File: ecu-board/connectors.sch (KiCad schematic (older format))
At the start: 19 parts, among them J10 Injector connector, J11 MAP connector, J13 Chrankshaft Hall connector, J14 Camshaft Hall connector, J15 EGO connector, J2 Battery power conenctor, J3 Button input connector, J4 Motor conenctor, J5 Serial DB9 connector, J6 Ignition 1 connector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

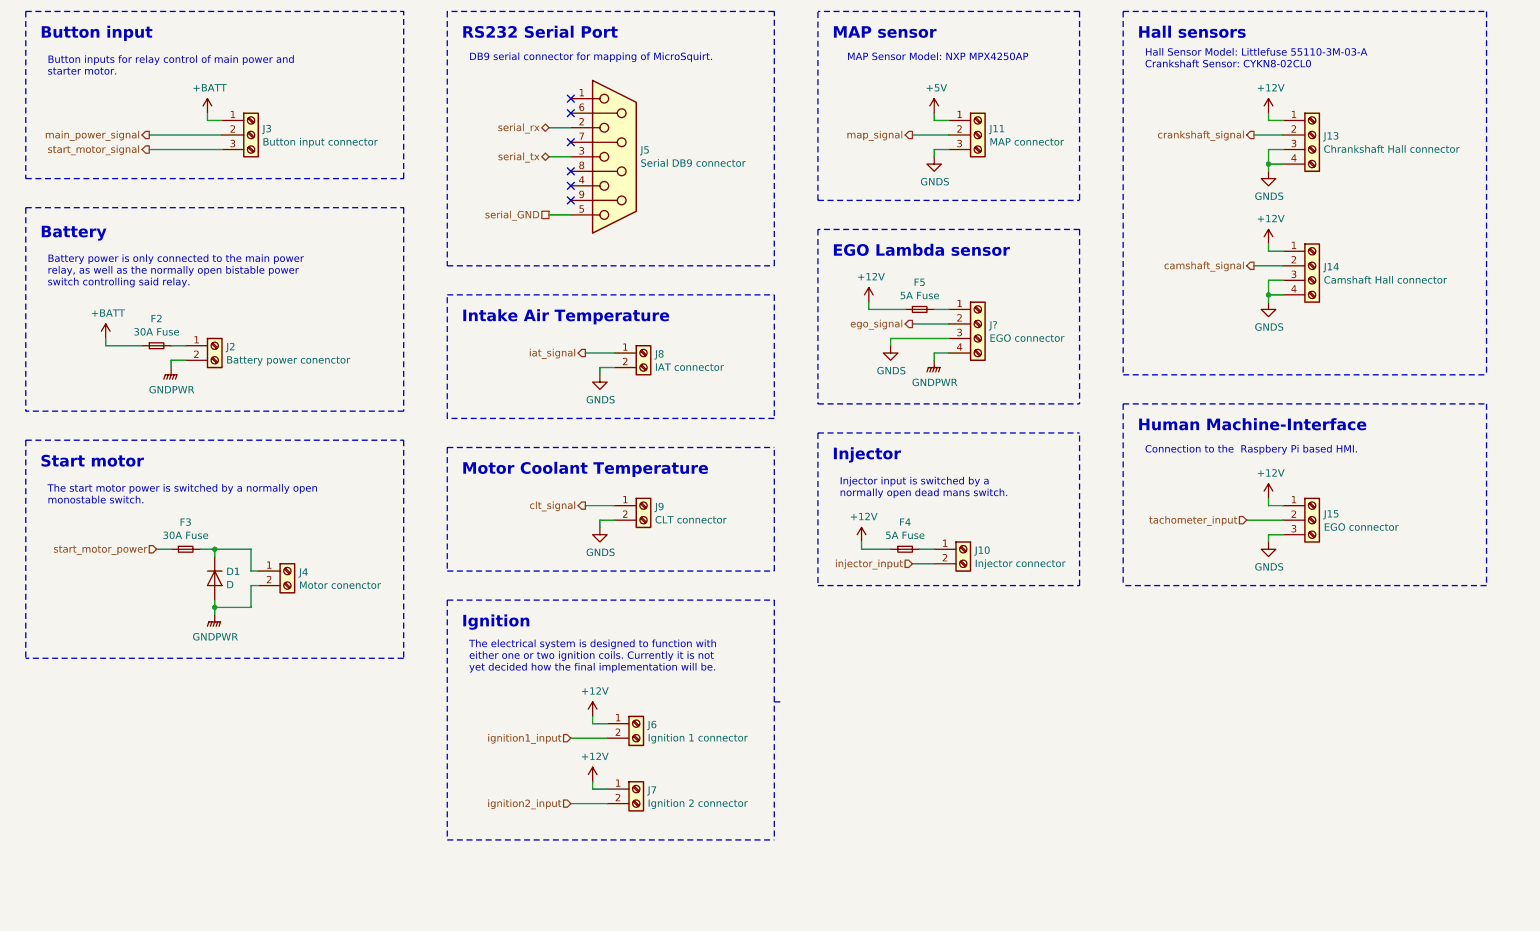
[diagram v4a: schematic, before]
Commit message: Mount MAP sensor to PCB. Reverse injector input.
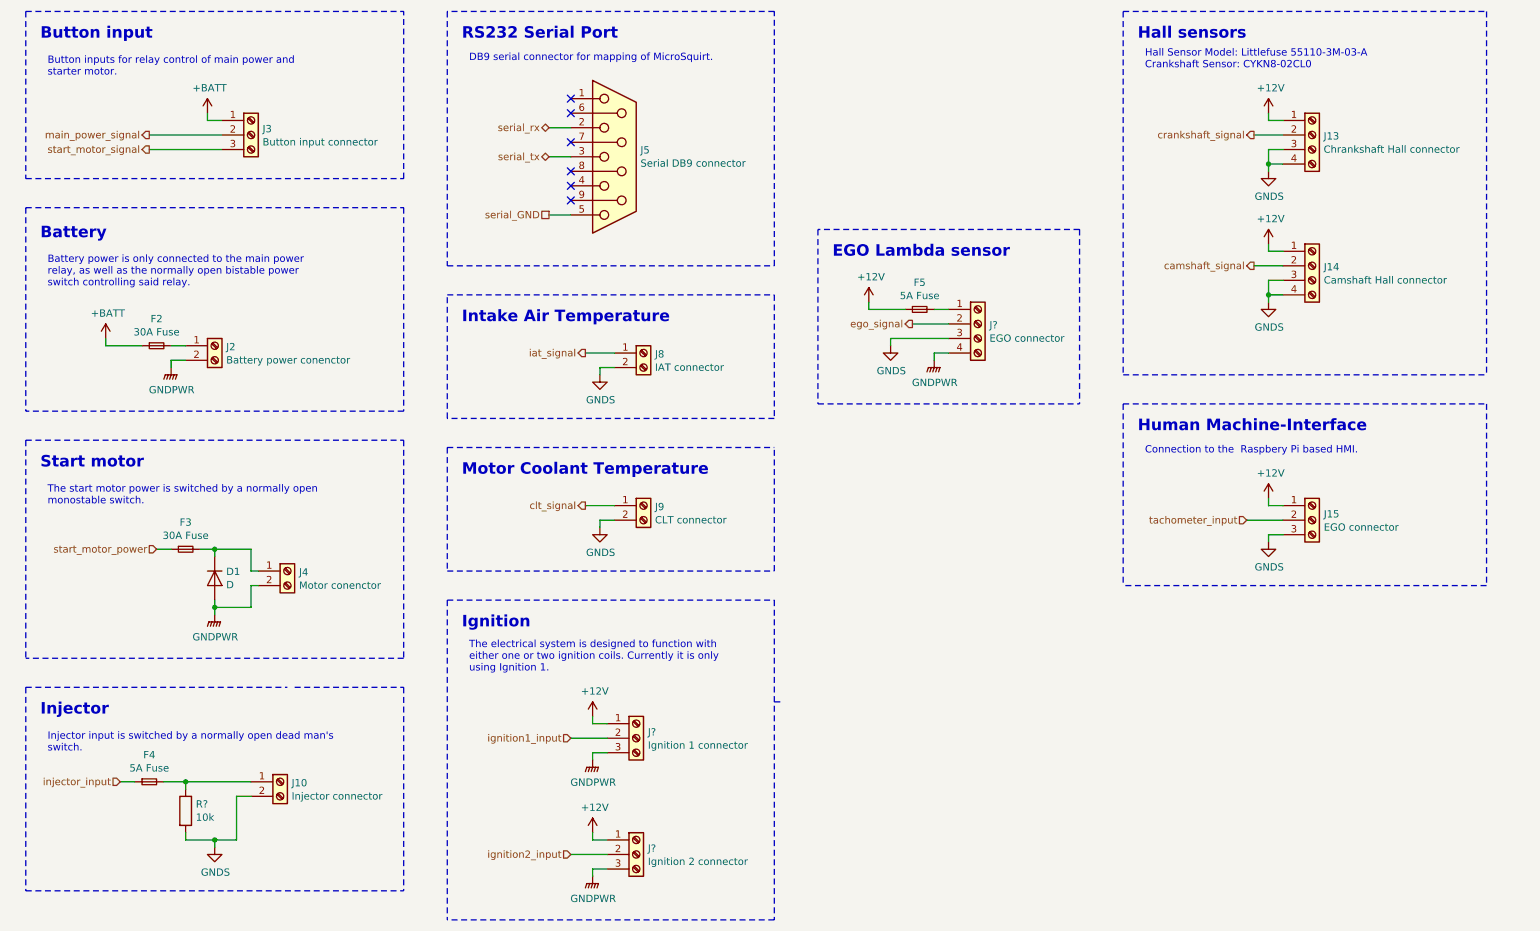
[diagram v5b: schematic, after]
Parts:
- removed J11: MAP connector, symbol Connector:Screw_Terminal_01x03
- removed J6: Ignition 1 connector, symbol Connector:Screw_Terminal_01x02
- removed J7: Ignition 2 connector, symbol Connector:Screw_Terminal_01x02
- added J?: Ignition 1 connector, symbol Connector:Screw_Terminal_01x03
- added J?: Ignition 2 connector, symbol Connector:Screw_Terminal_01x03
- added R?: 10k, symbol Device:R
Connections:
- net +12V: now also J?.1 (Pin_1), J?.1 (Pin_1); no longer F4.1
- net GNDPWR: now also J?.3 (Pin_3), J?.3 (Pin_3)
- net GNDS: now also J10.2 (Pin_2), R?.2
- net ignition1_input: now also J?.2 (Pin_2)
- net ignition2_input: now also J?.2 (Pin_2)
- net injector_input: now also F4.1; no longer J10.2 (Pin_2)
- net at F4.2, J10.1 (Pin_1): now also R?.1
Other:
- note added: "Injector input is switched by a normally open dead man's \nswitch."
- note added: "The electrical system is designed to function with \neither one or two ignition coils. Currently it is only \nusing Ignition 1."
- note removed: "Injector input is switched by a \nnormally open dead mans switch."
- note removed: "MAP Sensor Model: NXP MPX4250AP"
- note removed: "MAP sensor"
- note removed: "The electrical system is designed to function with \neither one or two ignition coils. Currently it is not \nyet decided how the final implementation will be."
- moved on the sheet: F4, J10
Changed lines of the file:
@@
 Wire Notes Line
 	8350 900  8350 3400
-Text Notes 6350 1100 0    79   ~ 16
-MAP sensor
 Wire Notes Line
 	8350 3400 10850 3400
 Wire Notes Line
 	8350 900  10850 900
-$Comp
-L power:+5V #PWR017
-U 1 1 5C573391
-P 7050 1600
-F 0 "#PWR017" H 7050 1450 50  0001 C CNN
-F 1 "+5V" H 7065 1773 50  0000 C CNN
-F 2 "" H 7050 1600 50  0001 C CNN
-F 3 "" H 7050 1600 50  0001 C CNN
-	1    7050 1600
-	1    0    0    -1
-$EndComp
-Wire Wire Line
-	7050 1600 7050 1650
-Wire Wire Line
-	7050 1650 7150 1650
-$Comp
-L power:GNDS #PWR018
-U 1 1 5C57367C
-P 7050 1900
-F 0 "#PWR018" H 7050 1650 50  0001 C CNN
-F 1 "GNDS" H 7055 1727 50  0000 C CNN
-F 2 "" H 7050 1900 50  0001 C CNN
-F 3 "" H 7050 1900 50  0001 C CNN
-	1    7050 1900
-	1    0    0    -1
-$EndComp
-Wire Wire Line
-	7050 1900 7050 1850
-Text Notes 6450 1250 0    50   ~ 0
-MAP Sensor Model: NXP MPX4250AP
-Wire Notes Line
-	8050 900  8050 2200
-Wire Notes Line
-	6250 2200 6250 900
-Wire Notes Line
-	8050 900  6250 900
-Wire Notes Line
-	6250 2200 8050 2200
 Wire Wire Line
 	9250 1750 9450 1750
@@
 Text HLabel 9250 2650 0    50   Output ~ 0
 camshaft_signal
-Text HLabel 6900 1750 0    50   Output ~ 0
-map_signal
 Text Notes 6350 2600 0    79   ~ 16
 EGO Lambda sensor
@@
 Wire Notes Line
 	3700 900  3700 2650
-Text Notes 6350 4000 0    79   ~ 16
+Text Notes 900  5750 0    79   ~ 16
 Injector\n
 Wire Notes Line
-	6250 3800 8050 3800
-$Comp
-L power:+12V #PWR015
-U 1 1 5C57FB87
-P 6550 4550
-F 0 "#PWR015" H 6550 4400 50  0001 C CNN
-F 1 "+12V" H 6565 4723 50  0000 C CNN
-F 2 "" H 6550 4550 50  0001 C CNN
-F 3 "" H 6550 4550 50  0001 C CNN
-	1    6550 4550
-	1    0    0    -1
-$EndComp
-Text HLabel 6900 4700 0    50   Input ~ 0
+	800  5550 2600 5550
+Text HLabel 1450 6200 0    50   Input ~ 0
 injector_input
-Wire Wire Line
-	6900 4700 7050 4700
-Wire Notes Line
-	6250 3800 6250 4850
-Wire Notes Line
-	6250 4850 8050 4850
-Wire Notes Line
-	8050 4850 8050 3800
-Text Notes 6400 4250 0    50   ~ 0
-Injector input is switched by a \nnormally open dead mans switch.
+Text Notes 950  6000 0    50   ~ 0
+Injector input is switched by a normally open dead man's \nswitch.
 Text Notes 3800 4100 0    79   ~ 16
 Motor Coolant Temperature\n
@@
 L Connector:Screw_Terminal_01x02 J10
 U 1 1 5C594BAE
-P 7250 4600
-F 0 "J10" H 7329 4592 50  0000 L CNN
-F 1 "Injector connector" H 7329 4501 50  0000 L CNN
-F 2 "" H 7250 4600 50  0001 C CNN
-F 3 "~" H 7250 4600 50  0001 C CNN
-F 4 "2314998, 2315061" H 7250 4600 50  0001 C CNN "Farnell"
-	1    7250 4600
+P 2550 6200
+F 0 "J10" H 2629 6192 50  0000 L CNN
+F 1 "Injector connector" H 2629 6101 50  0000 L CNN
+F 2 "" H 2550 6200 50  0001 C CNN
+F 3 "~" H 2550 6200 50  0001 C CNN
+F 4 "2314998, 2315061" H 2550 6200 50  0001 C CNN "Farnell"
+	1    2550 6200
 	1    0    0    -1
 $EndComp
@@
 L Device:Fuse_Small F4
 U 1 1 5C5BEADD
-P 6850 4600
-F 0 "F4" H 6850 4785 50  0000 C CNN
-F 1 "5A Fuse" H 6850 4694 50  0000 C CNN
-F 2 "" H 6850 4600 50  0001 C CNN
-F 3 "~" H 6850 4600 50  0001 C CNN
-F 4 "2292904" H 50  100 50  0001 C CNN "Farnell"
-	1    6850 4600
-	1    0    0    -1
-$EndComp
-Wire Wire Line
-	7050 4600 6950 4600
-Wire Wire Line
-	6750 4600 6550 4600
-Wire Wire Line
-	6550 4600 6550 4550
+P 1650 6200
+F 0 "F4" H 1650 6385 50  0000 C CNN
+F 1 "5A Fuse" H 1650 6294 50  0000 C CNN
+F 2 "" H 1650 6200 50  0001 C CNN
+F 3 "~" H 1650 6200 50  0001 C CNN
+F 4 "2292904" H -5150 1700 50  0001 C CNN "Farnell"
+	1    1650 6200
+	1    0    0    -1
+$EndComp
 $Comp
 L Connector:Screw_Terminal_01x02 J2
@@
 Wire Notes Line
 	5950 5650 6000 5650
-$Comp
-L Connector:Screw_Terminal_01x02 J6
-U 1 1 5C6199D0
-P 5000 5800
-F 0 "J6" H 5079 5792 50  0000 L CNN
-F 1 "Ignition 1 connector" H 5079 5701 50  0000 L CNN
-F 2 "" H 5000 5800 50  0001 C CNN
-F 3 "~" H 5000 5800 50  0001 C CNN
-F 4 "2314998, 2315061" H 5000 5800 50  0001 C CNN "Farnell"
-	1    5000 5800
-	1    0    0    -1
-$EndComp
-$Comp
-L Connector:Screw_Terminal_01x02 J7
-U 1 1 5C619A32
-P 5000 6250
-F 0 "J7" H 5079 6242 50  0000 L CNN
-F 1 "Ignition 2 connector" H 5079 6151 50  0000 L CNN
-F 2 "" H 5000 6250 50  0001 C CNN
-F 3 "~" H 5000 6250 50  0001 C CNN
-F 4 "2314998, 2315061" H 5000 6250 50  0001 C CNN "Farnell"
-	1    5000 6250
-	1    0    0    -1
-$EndComp
 Text Notes 3850 5450 0    50   ~ 0
-The electrical system is designed to function with \neither one or two ignition coils. Currently it is not \nyet decided how the final implementation will be.
+The electrical system is designed to function with \neither one or two ignition coils. Currently it is only \nusing Ignition 1.
 $Comp
 L power:+12V #PWR011
@@
 L power:+12V #PWR012
 U 1 1 5C62A8FD
-P 4700 6200
-F 0 "#PWR012" H 4700 6050 50  0001 C CNN
-F 1 "+12V" H 4715 6373 50  0000 C CNN
-F 2 "" H 4700 6200 50  0001 C CNN
-F 3 "" H 4700 6200 50  0001 C CNN
-	1    4700 6200
-	1    0    0    -1
-$EndComp
-Wire Wire Line
-	4700 6200 4700 6250
-Wire Wire Line
-	4700 6250 4800 6250
+P 4700 6550
+F 0 "#PWR012" H 4700 6400 50  0001 C CNN
+F 1 "+12V" H 4715 6723 50  0000 C CNN
+F 2 "" H 4700 6550 50  0001 C CNN
+F 3 "" H 4700 6550 50  0001 C CNN
+	1    4700 6550
+	1    0    0    -1
+$EndComp
+Wire Wire Line
+	4700 6550 4700 6600
+Wire Wire Line
+	4700 6600 4800 6600
 Text HLabel 4550 5900 0    50   Input ~ 0
 ignition1_input
-Text HLabel 4550 6350 0    50   Input ~ 0
+Text HLabel 4550 6700 0    50   Input ~ 0
 ignition2_input
 Wire Wire Line
 	4550 5900 4800 5900
 Wire Wire Line
-	4800 6350 4550 6350
-Wire Notes Line
-	3700 6600 5950 6600
-Wire Notes Line
-	5950 4950 5950 6600
-Wire Notes Line
-	3700 4950 3700 6600
+	4800 6700 4550 6700
 Wire Wire Line
 	4400 2300 4550 2300
@@
 	1    0    0    -1
 $EndComp
-Wire Wire Line
-	6900 1750 7150 1750
-Wire Wire Line
-	7050 1850 7150 1850
-$Comp
-L Connector:Screw_Terminal_01x03 J11
-U 1 1 5C59507A
-P 7350 1750
-F 0 "J11" H 7430 1792 50  0000 L CNN
-F 1 "MAP connector" H 7430 1701 50  0000 L CNN
-F 2 "" H 7350 1750 50  0001 C CNN
-F 3 "http://www.farnell.com/datasheets/2308387.pdf?_ga=2.20224184.1892952727.1549112209-881392492.1520553087" H 7350 1750 50  0001 C CNN
-F 4 "2315020, 2315083" H 7350 1750 50  0001 C CNN "Farnell"
-	1    7350 1750
-	1    0    0    -1
-$EndComp
 $Comp
 L power:GNDPWR #PWR?
@@
 Wire Notes Line
 	800  900  800  2050
+$Comp
+L Connector:Screw_Terminal_01x03 J?
+U 1 1 5C773356
+P 5000 5900
+F 0 "J?" H 5080 5942 50  0000 L CNN
+F 1 "Ignition 1 connector" H 5080 5851 50  0000 L CNN
+F 2 "" H 5000 5900 50  0001 C CNN
+F 3 "http://www.farnell.com/datasheets/2308387.pdf?_ga=2.20224184.1892952727.1549112209-881392492.1520553087" H 5000 5900 50  0001 C CNN
+F 4 "2315020, 2315083" H 5000 5900 50  0001 C CNN "Farnell"
+	1    5000 5900
+	1    0    0    -1
+$EndComp
+$Comp
+L Connector:Screw_Terminal_01x03 J?
+U 1 1 5C77363A
+P 5000 6700
+F 0 "J?" H 5080 6742 50  0000 L CNN
+F 1 "Ignition 2 connector" H 5080 6651 50  0000 L CNN
+F 2 "" H 5000 6700 50  0001 C CNN
+F 3 "http://www.farnell.com/datasheets/2308387.pdf?_ga=2.20224184.1892952727.1549112209-881392492.1520553087" H 5000 6700 50  0001 C CNN
+F 4 "2315020, 2315083" H 5000 6700 50  0001 C CNN "Farnell"
+	1    5000 6700
+	1    0    0    -1
+$EndComp
+$Comp
+L power:GNDPWR #PWR?
+U 1 1 5C77A9F8
+P 4700 6050
+F 0 "#PWR?" H 4700 5850 50  0001 C CNN
+F 1 "GNDPWR" H 4704 5896 50  0000 C CNN
+F 2 "" H 4700 6000 50  0001 C CNN
+F 3 "" H 4700 6000 50  0001 C CNN
+	1    4700 6050
+	1    0    0    -1
+$EndComp
+Wire Wire Line
+	4700 6050 4700 6000
+Wire Wire Line
+	4700 6000 4800 6000
+$Comp
+L power:GNDPWR #PWR?
+U 1 1 5C77CEFF
+P 4700 6850
+F 0 "#PWR?" H 4700 6650 50  0001 C CNN
+F 1 "GNDPWR" H 4704 6696 50  0000 C CNN
+F 2 "" H 4700 6800 50  0001 C CNN
+F 3 "" H 4700 6800 50  0001 C CNN
+	1    4700 6850
+	1    0    0    -1
+$EndComp
+Wire Wire Line
+	4700 6850 4700 6800
+Wire Wire Line
+	4700 6800 4800 6800
+Wire Notes Line
+	5950 7150 3700 7150
+Wire Notes Line
+	5950 4950 5950 7150
+Wire Notes Line
+	3700 4950 3700 7150
+$Comp
+L power:GNDS #PWR?
+U 1 1 5C783863
+P 2100 6650
+F 0 "#PWR?" H 2100 6400 50  0001 C CNN
+F 1 "GNDS" H 2105 6477 50  0000 C CNN
+F 2 "" H 2100 6650 50  0001 C CNN
+F 3 "" H 2100 6650 50  0001 C CNN
+	1    2100 6650
+	1    0    0    -1
+$EndComp
+$Comp
+L Device:R R?
+U 1 1 5C7A1D9C
+P 1900 6400
+F 0 "R?" H 1970 6446 50  0000 L CNN
+F 1 "10k" H 1970 6355 50  0000 L CNN
+F 2 "" V 1830 6400 50  0001 C CNN
+F 3 "~" H 1900 6400 50  0001 C CNN
+	1    1900 6400
+	1    0    0    -1
+$EndComp
+Wire Wire Line
+	1900 6250 1900 6200
+Wire Wire Line
+	1450 6200 1550 6200
+Wire Wire Line
+	2350 6300 2250 6300
+Wire Wire Line
+	2100 6650 2100 6600
+Wire Wire Line
+	2100 6600 1900 6600
+Wire Wire Line
+	1900 6600 1900 6550
+Wire Wire Line
+	2100 6600 2250 6600
+Wire Wire Line
+	2250 6300 2250 6600
+Connection ~ 2100 6600
+Wire Notes Line
+	800  5550 800  6950
+Wire Notes Line
+	3400 5550 3400 6950
+Wire Notes Line
+	2650 5550 3400 5550
+Wire Notes Line
+	800  6950 3400 6950
+Connection ~ 1900 6200
+Wire Wire Line
+	1750 6200 1900 6200
+Wire Wire Line
+	1900 6200 2350 6200
 $EndSCHEMATC

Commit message: Cockpit connector expanded and merged with button connector. Injector connected to dead man's switch.
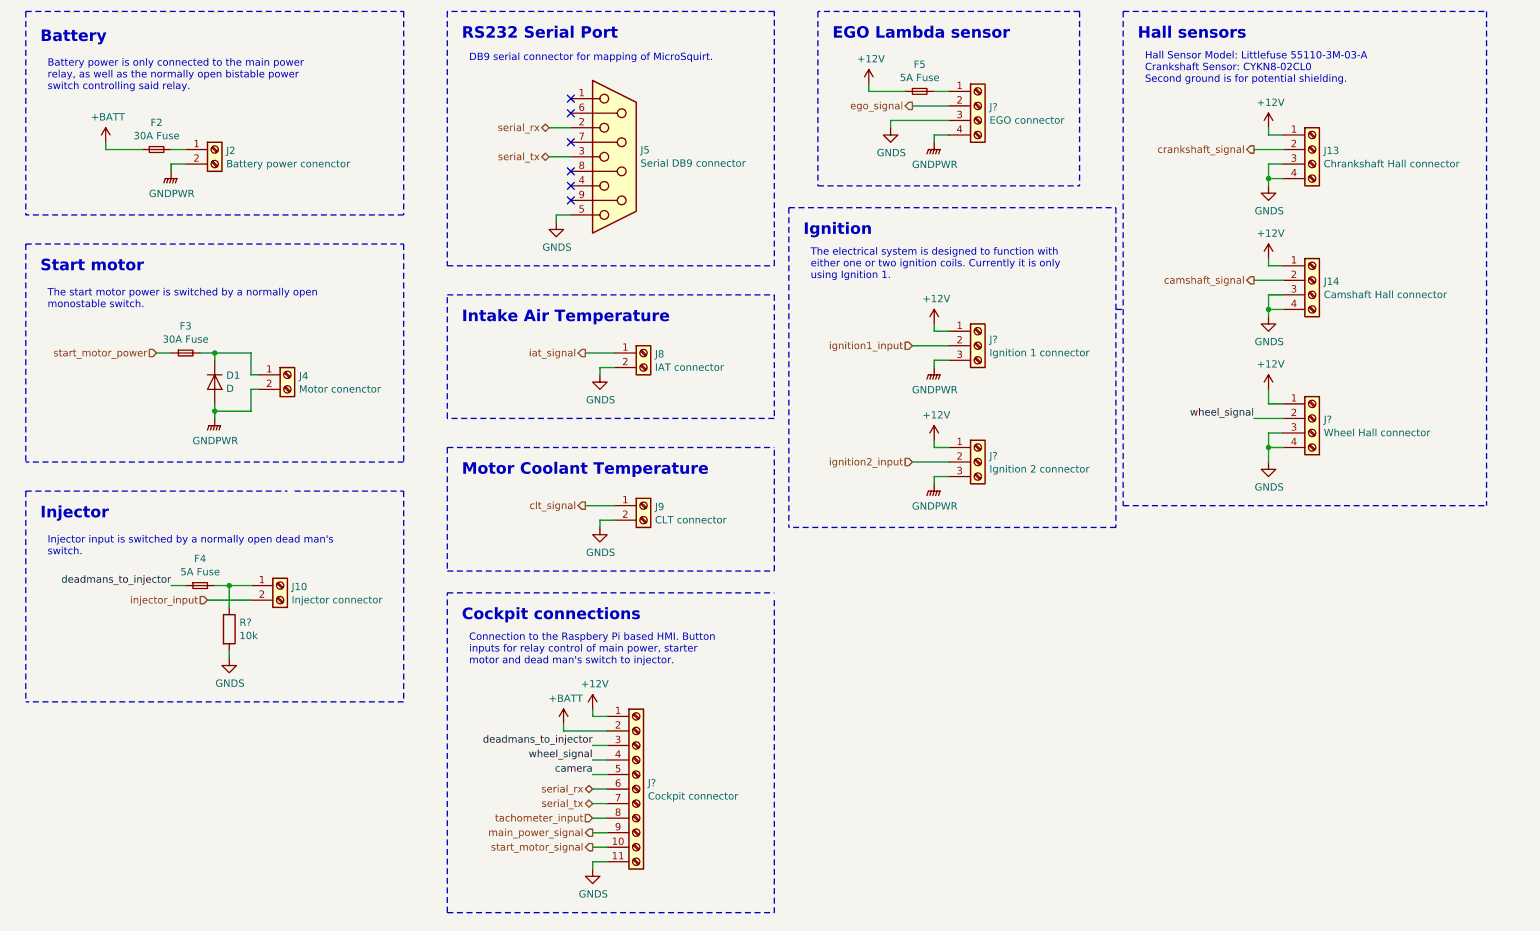
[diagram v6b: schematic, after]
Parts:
- removed J15: EGO connector, symbol Connector:Screw_Terminal_01x03
- removed J3: Button input connector, symbol Connector:Screw_Terminal_01x03
- added J?: Wheel Hall connector, symbol Connector:Screw_Terminal_01x04
- added J?: Cockpit connector, symbol Connector:Screw_Terminal_01x11
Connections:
- net serial_GND is gone; now on net GNDS: J5.5
- net +12V: now also J?.1 (Pin_1), J?.1 (Pin_1)
- net +BATT: now also J?.2 (Pin_2)
- net GNDS: now also J?.11 (Pin_11), J?.3 (Pin_3), J?.4 (Pin_4); no longer J10.2 (Pin_2)
- net injector_input: now also J10.2 (Pin_2); no longer F4.1
- net main_power_signal: now also J?.9 (Pin_9)
- net serial_rx: now also J?.6 (Pin_6)
- net serial_tx: now also J?.7 (Pin_7)
- net start_motor_signal: now also J?.10 (Pin_10)
- net tachometer_input: now also J?.8 (Pin_8)
- new net camera: J?.5 (Pin_5)
- new net deadmans_to_injector: F4.1, J?.3 (Pin_3)
- new net wheel_signal: J?.2 (Pin_2), J?.4 (Pin_4)
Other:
- note added: "Cockpit connections\n"
- note added: "Connection to the Raspbery Pi based HMI. Button \ninputs for relay control of main power, starter \nmotor and dead man's switch to injector."
- note added: "Hall Sensor Model: Littlefuse 55110-3M-03-A\nCrankshaft Sensor: CYKN8-02CL0\nSecond ground is for potential shielding."
- note removed: "Button input\n"
- note removed: "Button inputs for relay control of main power and \nstarter motor."
- note removed: "Connection to the Raspbery Pi based HMI.\n"
- note removed: "Hall Sensor Model: Littlefuse 55110-3M-03-A\nCrankshaft Sensor: CYKN8-02CL0"
- note removed: "Human Machine-Interface"
- moved on the sheet: D1, F2, F3, F4, F5, J10, J13, J14, J2, J4, J?, R?
